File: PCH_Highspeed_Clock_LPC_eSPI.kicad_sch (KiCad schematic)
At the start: 3 parts

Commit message: Restructured schematic
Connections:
- net PCH_x4_Refclk-: now reaches UPCH1.AE14 (CLKOUT_PCIE_N2)
- net PCH_x4_Refclk+: now reaches UPCH1.AE15 (CLKOUT_PCIE_P2)
- net PCH_x4_CLKREQ#: now reaches UPCH1.AR32 (GPP_B7/SRCCLKREQ2#)
- net PCH_x4_PCIe_Tx0+: now reaches UPCH1.F46 (PCIE21_TXP)
- net PCH_x4_PCIe_Tx3+: now reaches UPCH1.G45 (PCIE24_TXP)
- net PCH_x4_PCIe_Tx3-: now reaches UPCH1.G46 (PCIE24_TXN)
- net PCH_x4_PCIe_Tx0-: now reaches UPCH1.G47 (PCIE21_TXN)
- net PCH_x4_PCIe_Tx2+: now reaches UPCH1.G48 (PCIE23_TXP)
- net PCH_x4_PCIe_Tx2-: now reaches UPCH1.G49 (PCIE23_TXN)
- net PCH_x4_PCIe_Tx1-: now reaches UPCH1.H47 (PCIE22_TXN)
- net PCH_x4_PCIe_Tx1+: now reaches UPCH1.H48 (PCIE22_TXP)
- net PCH_x4_PCIe_Rx0+: now reaches UPCH1.R44 (PCIE21_RXP)
- net PCH_x4_PCIe_Rx0-: now reaches UPCH1.T43 (PCIE21_RXN)
- net PCH_x4_PCIe_Rx1-: now reaches UPCH1.U40 (PCIE22_RXN)
- net PCH_x4_PCIe_Rx1+: now reaches UPCH1.U41 (PCIE22_RXP)
- net PCH_x4_PCIe_Rx2-: now reaches UPCH1.W43 (PCIE23_RXN)
- net PCH_x4_PCIe_Rx2+: now reaches UPCH1.W44 (PCIE23_RXP)
- net PCH_x4_PCIe_Rx3-: now reaches UPCH1.Y40 (PCIE24_RXN)
- net PCH_x4_PCIe_Rx3+: now reaches UPCH1.Y41 (PCIE24_RXP)
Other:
- note added: "Keep CLKREQ# and Refclk+/- paired!"
- note added: "subtract 5 for PCIe lane number (first 6 lanes are the USB3.1G2 ports + index starts at 0 vs 1)"
- note removed: "subtract 5 for PCIe lane number (first 6 lanes are the USB3.2G2 ports + index starts at 0 vs 1)"

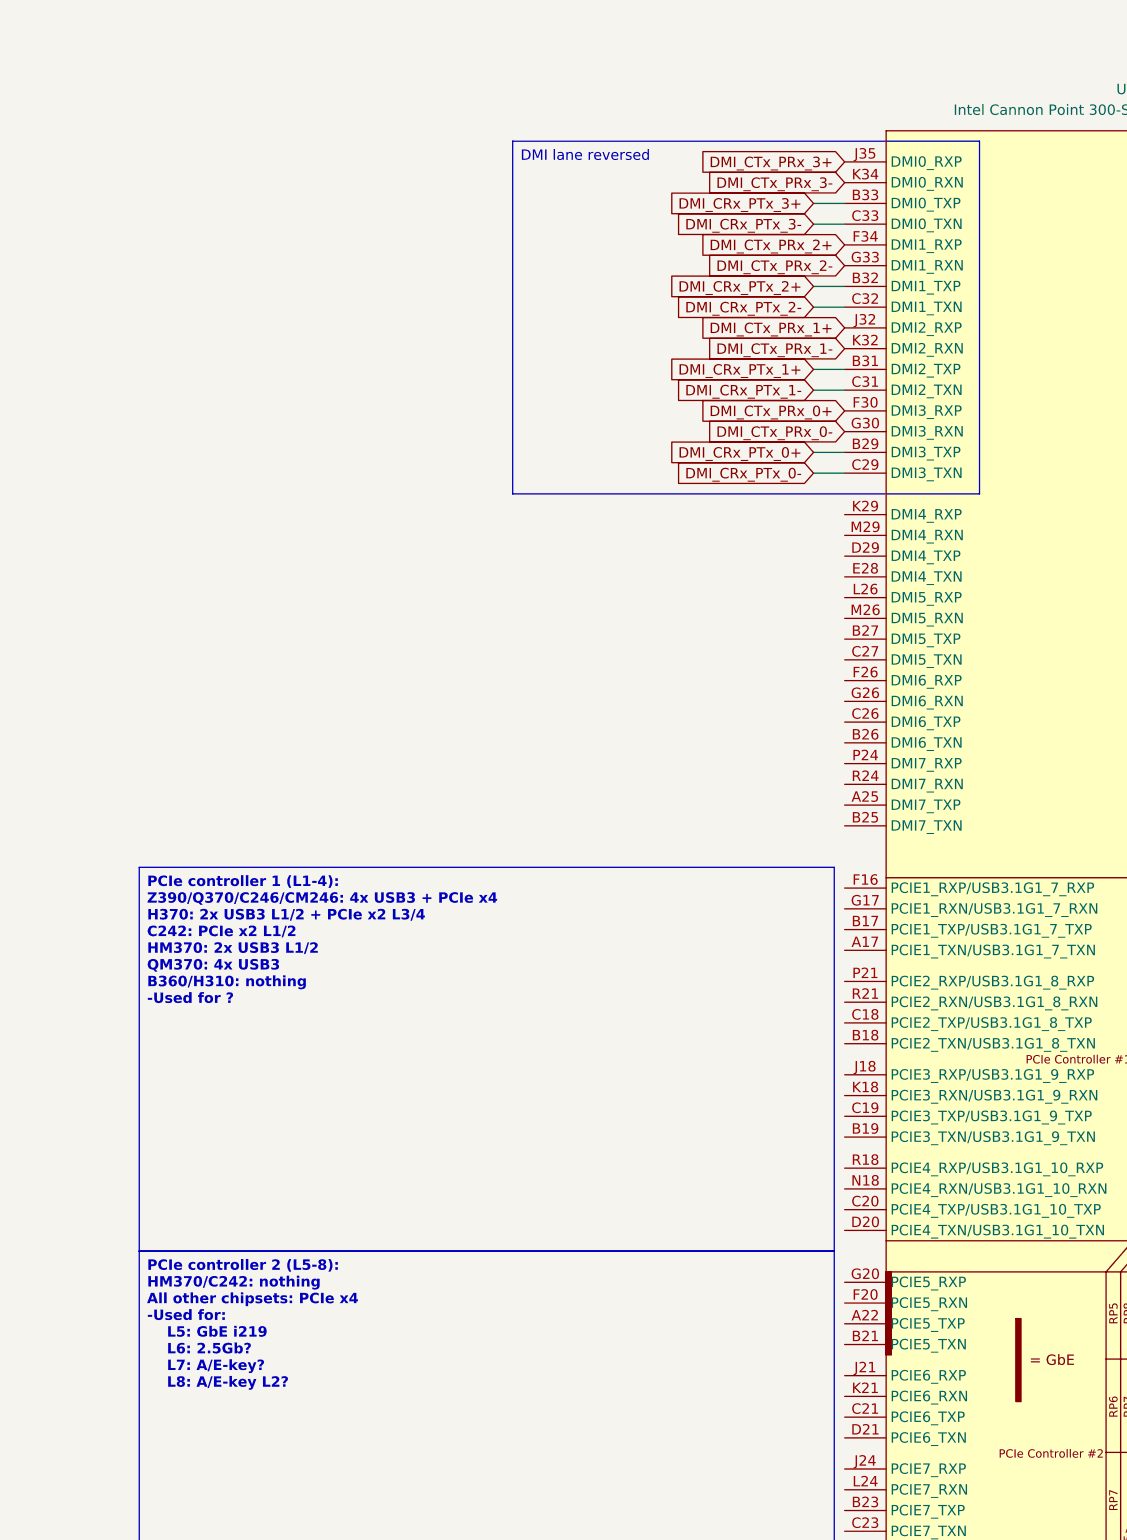
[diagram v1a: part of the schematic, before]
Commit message: Added interconnect between CPU and PCH boards and added ATX board outline
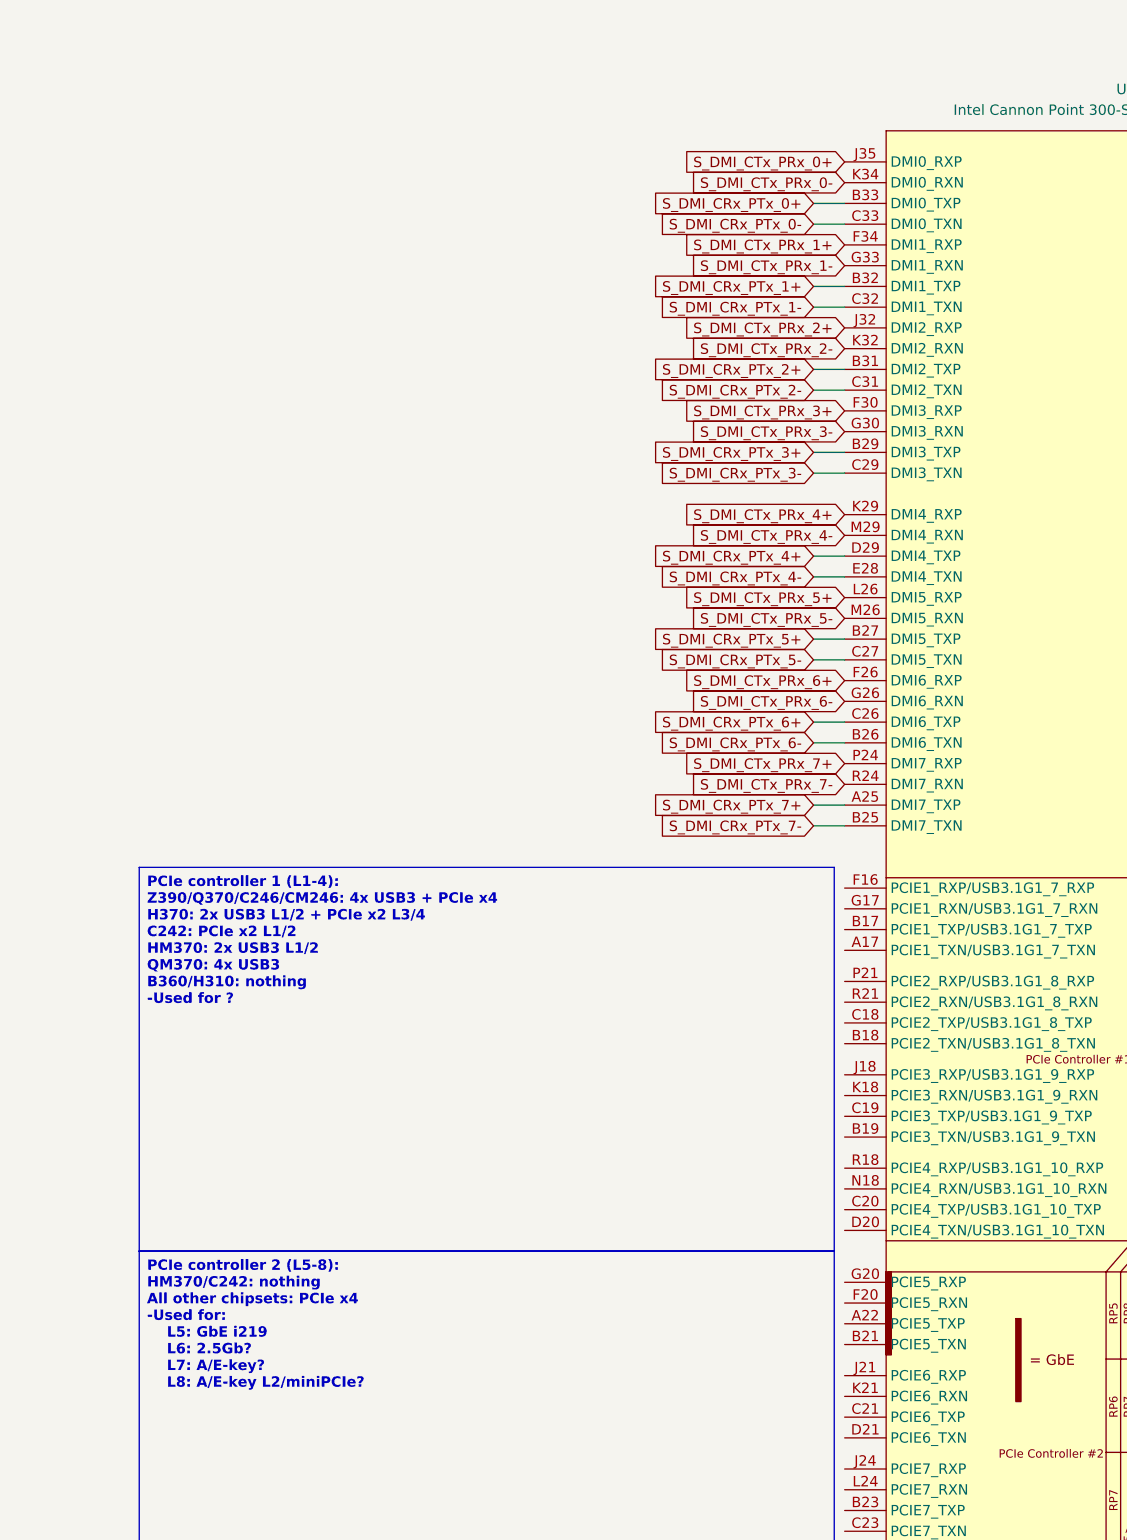
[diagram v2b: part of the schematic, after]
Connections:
- net S_DMI_CRx_PTx_7+: now reaches UPCH1.A25 (DMI7_TXP)
- net S_DMI_CRx_PTx_7-: now reaches UPCH1.B25 (DMI7_TXN)
- net S_DMI_CRx_PTx_6-: now reaches UPCH1.B26 (DMI6_TXN)
- net S_DMI_CRx_PTx_5+: now reaches UPCH1.B27 (DMI5_TXP)
- net S_DMI_CRx_PTx_6+: now reaches UPCH1.C26 (DMI6_TXP)
- net S_DMI_CRx_PTx_5-: now reaches UPCH1.C27 (DMI5_TXN)
- net S_DMI_CRx_PTx_4+: now reaches UPCH1.D29 (DMI4_TXP)
- net S_DMI_CRx_PTx_4-: now reaches UPCH1.E28 (DMI4_TXN)
- net S_DMI_CTx_PRx_6+: now reaches UPCH1.F26 (DMI6_RXP)
- net S_DMI_CTx_PRx_6-: now reaches UPCH1.G26 (DMI6_RXN)
- net S_DMI_CTx_PRx_4+: now reaches UPCH1.K29 (DMI4_RXP)
- net S_DMI_CTx_PRx_5+: now reaches UPCH1.L26 (DMI5_RXP)
- net S_DMI_CTx_PRx_5-: now reaches UPCH1.M26 (DMI5_RXN)
- net S_DMI_CTx_PRx_4-: now reaches UPCH1.M29 (DMI4_RXN)
- net S_DMI_CTx_PRx_7+: now reaches UPCH1.P24 (DMI7_RXP)
- net S_DMI_CTx_PRx_7-: now reaches UPCH1.R24 (DMI7_RXN)
- net DMI_CRx_PTx_0+ renamed S_DMI_CRx_PTx_3+
- net DMI_CRx_PTx_0- renamed S_DMI_CRx_PTx_3-
- net DMI_CRx_PTx_1+ renamed S_DMI_CRx_PTx_2+
- net DMI_CRx_PTx_1- renamed S_DMI_CRx_PTx_2-
- net DMI_CRx_PTx_2+ renamed S_DMI_CRx_PTx_1+
- net DMI_CRx_PTx_2- renamed S_DMI_CRx_PTx_1-
- net DMI_CRx_PTx_3+ renamed S_DMI_CRx_PTx_0+
- net DMI_CRx_PTx_3- renamed S_DMI_CRx_PTx_0-
- net DMI_CTx_PRx_0+ renamed S_DMI_CTx_PRx_3+
- net DMI_CTx_PRx_0- renamed S_DMI_CTx_PRx_3-
- net DMI_CTx_PRx_1+ renamed S_DMI_CTx_PRx_2+
- net DMI_CTx_PRx_1- renamed S_DMI_CTx_PRx_2-
- net DMI_CTx_PRx_2+ renamed S_DMI_CTx_PRx_1+
- net DMI_CTx_PRx_2- renamed S_DMI_CTx_PRx_1-
- net DMI_CTx_PRx_3+ renamed S_DMI_CTx_PRx_0+
- net DMI_CTx_PRx_3- renamed S_DMI_CTx_PRx_0-

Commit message: Added more PCIe slots and mounting holes
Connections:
- net PCH_x4_1_Refclk-: now reaches UPCH1.AB2 (CLKOUT_PCIE_N5)
- net PCH_x4_1_Refclk+: now reaches UPCH1.AB3 (CLKOUT_PCIE_P5)
- net PCH_x4_4_Refclk-: now reaches UPCH1.AC2 (CLKOUT_PCIE_N4)
- net PCH_x4_4_Refclk+: now reaches UPCH1.AC3 (CLKOUT_PCIE_P4)
- net PCH_x4_5_Refclk-: now reaches UPCH1.AE6 (CLKOUT_PCIE_N3)
- net PCH_x4_5_Refclk+: now reaches UPCH1.AE7 (CLKOUT_PCIE_P3)
- net PCH_x4_1_CLKREQ#: now reaches UPCH1.AN29 (GPP_B10/SRCCLKREQ5#)
- net PCH_x4_4_CLKREQ#: now reaches UPCH1.BA30 (GPP_B9/SRCCLKREQ4#)
- net PCH_x4_5_CLKREQ#: now reaches UPCH1.BB30 (GPP_B8/SRCCLKREQ3#)
- net PCH_x4_5_PCIe_Tx0-: now reaches UPCH1.A42 (PCIE17_TXN/SATA4_TXN)
- net PCH_x4_5_PCIe_Tx3-: now reaches UPCH1.A44 (PCIE20_TXN/SATA7_TXN)
- net PCH_x4_4_PCIe_Rx0-: now reaches UPCH1.B38 (PCIE13_TXN/SATA0B_TXN)
- net PCH_x4_4_PCIe_Rx2-: now reaches UPCH1.B40 (PCIE15_TXN/SATA2_TXN)
- net PCH_x4_4_PCIe_Rx3-: now reaches UPCH1.B41 (PCIE16_TXN/SATA3_TXN)
- net PCH_x4_5_PCIe_Tx0+: now reaches UPCH1.B42 (PCIE17_TXP/SATA4_TXP)
- net PCH_x4_5_PCIe_Tx3+: now reaches UPCH1.B44 (PCIE20_TXP/SATA7_TXP)
- net PCH_x4_4_PCIe_Rx0+: now reaches UPCH1.C38 (PCIE13_TXP/SATA0B_TXP)
- net PCH_x4_4_PCIe_Rx1-: now reaches UPCH1.C39 (PCIE14_TXN/SATA1B_TXN)
- net PCH_x4_4_PCIe_Rx2+: now reaches UPCH1.C40 (PCIE15_TXP/SATA2_TXP)
- net PCH_x4_4_PCIe_Rx3+: now reaches UPCH1.C41 (PCIE16_TXP/SATA3_TXP)
- net PCH_x4_5_PCIe_Tx1-: now reaches UPCH1.C42 (PCIE18_TXN/SATA5_TXN)
- net PCH_x4_5_PCIe_Tx2-: now reaches UPCH1.C44 (PCIE19_TXN/SATA6_TXN)
- net PCH_x4_4_PCIe_Tx0-: now reaches UPCH1.C45 (PCIE13_RXN/SATA0B_RXN)
- net PCH_x4_4_PCIe_Tx0+: now reaches UPCH1.C46 (PCIE13_RXP/SATA0B_RXP)
- net PCH_x4_4_PCIe_Tx1+: now reaches UPCH1.C47 (PCIE14_RXP/SATA1B_RXP)
- net PCH_x4_4_PCIe_Rx1+: now reaches UPCH1.D39 (PCIE14_TXP/SATA1B_TXP)
- net PCH_x4_5_PCIe_Tx1+: now reaches UPCH1.D42 (PCIE18_TXP/SATA5_TXP)
- net PCH_x4_5_PCIe_Tx2+: now reaches UPCH1.D43 (PCIE19_TXP/SATA6_TXP)
- net PCH_x4_4_PCIe_Tx1-: now reaches UPCH1.D46 (PCIE14_RXN/SATA1B_RXN)
- net PCH_x4_4_PCIe_Tx2+: now reaches UPCH1.E45 (PCIE15_RXP/SATA2_RXP)
- net PCH_x4_4_PCIe_Tx2-: now reaches UPCH1.F44 (PCIE15_RXN/SATA2_RXN)
- net PCH_x4_5_PCIe_Rx0-: now reaches UPCH1.K43 (PCIE17_RXN/SATA4_RXN)
- net PCH_x4_5_PCIe_Rx0+: now reaches UPCH1.K44 (PCIE17_RXP/SATA4_RXP)
- net PCH_x4_4_PCIe_Tx3-: now reaches UPCH1.L41 (PCIE16_RXN/SATA3_RXN)
- net PCH_x4_4_PCIe_Tx3+: now reaches UPCH1.M40 (PCIE16_RXP/SATA3_RXP)
- net PCH_x4_5_PCIe_Rx2-: now reaches UPCH1.M44 (PCIE19_RXN/SATA6_RXN)
- net PCH_x4_5_PCIe_Rx2+: now reaches UPCH1.N42 (PCIE19_RXP/SATA6_RXP)
- net PCH_x4_5_PCIe_Rx1-: now reaches UPCH1.P41 (PCIE18_RXN/SATA5_RXN)
- net PCH_x4_5_PCIe_Rx3-: now reaches UPCH1.R35 (PCIE20_RXN/SATA7_RXN)
- net PCH_x4_5_PCIe_Rx3+: now reaches UPCH1.R37 (PCIE20_RXP/SATA7_RXP)
- net PCH_x4_5_PCIe_Rx1+: now reaches UPCH1.R40 (PCIE18_RXP/SATA5_RXP)
- net PCH_x4_1_PCIe_Tx0-: now reaches UPCH1.A17 (PCIE1_TXN/USB3.1G1_7_TXN)
- net PCH_x4_1_PCIe_Tx0+: now reaches UPCH1.B17 (PCIE1_TXP/USB3.1G1_7_TXP)
- net PCH_x4_1_PCIe_Tx1-: now reaches UPCH1.B18 (PCIE2_TXN/USB3.1G1_8_TXN)
- net PCH_x4_1_PCIe_Tx2-: now reaches UPCH1.B19 (PCIE3_TXN/USB3.1G1_9_TXN)
- net PCH_x4_1_PCIe_Tx1+: now reaches UPCH1.C18 (PCIE2_TXP/USB3.1G1_8_TXP)
- net PCH_x4_1_PCIe_Tx2+: now reaches UPCH1.C19 (PCIE3_TXP/USB3.1G1_9_TXP)
- net PCH_x4_1_PCIe_Tx3+: now reaches UPCH1.C20 (PCIE4_TXP/USB3.1G1_10_TXP)
- net PCH_x4_1_PCIe_Tx3-: now reaches UPCH1.D20 (PCIE4_TXN/USB3.1G1_10_TXN)
- net PCH_x4_1_PCIe_Rx0+: now reaches UPCH1.F16 (PCIE1_RXP/USB3.1G1_7_RXP)
- net PCH_x4_1_PCIe_Rx0-: now reaches UPCH1.G17 (PCIE1_RXN/USB3.1G1_7_RXN)
- net PCH_x4_1_PCIe_Rx2+: now reaches UPCH1.J18 (PCIE3_RXP/USB3.1G1_9_RXP)
- net PCH_x4_1_PCIe_Rx2-: now reaches UPCH1.K18 (PCIE3_RXN/USB3.1G1_9_RXN)
- net PCH_x4_1_PCIe_Rx3-: now reaches UPCH1.N18 (PCIE4_RXN/USB3.1G1_10_RXN)
- net PCH_x4_1_PCIe_Rx1+: now reaches UPCH1.P21 (PCIE2_RXP/USB3.1G1_8_RXP)
- net PCH_x4_1_PCIe_Rx3+: now reaches UPCH1.R18 (PCIE4_RXP/USB3.1G1_10_RXP)
- net PCH_x4_1_PCIe_Rx1-: now reaches UPCH1.R21 (PCIE2_RXN/USB3.1G1_8_RXN)
- net PCH_x4_CLKREQ# renamed PCH_x4_6_CLKREQ#
- net PCH_x4_PCIe_Rx0+ renamed PCH_x4_6_PCIe_Rx0+
- net PCH_x4_PCIe_Rx0- renamed PCH_x4_6_PCIe_Rx0-
- net PCH_x4_PCIe_Rx1+ renamed PCH_x4_6_PCIe_Rx1+
- net PCH_x4_PCIe_Rx1- renamed PCH_x4_6_PCIe_Rx1-
- net PCH_x4_PCIe_Rx2+ renamed PCH_x4_6_PCIe_Rx2+
- net PCH_x4_PCIe_Rx2- renamed PCH_x4_6_PCIe_Rx2-
- net PCH_x4_PCIe_Rx3+ renamed PCH_x4_6_PCIe_Rx3+
- net PCH_x4_PCIe_Rx3- renamed PCH_x4_6_PCIe_Rx3-
- net PCH_x4_PCIe_Tx0+ renamed PCH_x4_6_PCIe_Tx0+
- net PCH_x4_PCIe_Tx0- renamed PCH_x4_6_PCIe_Tx0-
- net PCH_x4_PCIe_Tx1+ renamed PCH_x4_6_PCIe_Tx1+
- net PCH_x4_PCIe_Tx1- renamed PCH_x4_6_PCIe_Tx1-
- net PCH_x4_PCIe_Tx2+ renamed PCH_x4_6_PCIe_Tx2+
- net PCH_x4_PCIe_Tx2- renamed PCH_x4_6_PCIe_Tx2-
- net PCH_x4_PCIe_Tx3+ renamed PCH_x4_6_PCIe_Tx3+
- net PCH_x4_PCIe_Tx3- renamed PCH_x4_6_PCIe_Tx3-
- net PCH_x4_Refclk+ renamed PCH_x4_6_Refclk+
- net PCH_x4_Refclk- renamed PCH_x4_6_Refclk-
- net SSD0_PCIe/SATA_Rx0+ renamed SSD0_SATA/PCIe_Rx0+
- net SSD0_PCIe/SATA_Rx0- renamed SSD0_SATA/PCIe_Rx0-
- net SSD0_PCIe/SATA_Tx0+ renamed SSD0_SATA/PCIe_Tx0+
- net SSD0_PCIe/SATA_Tx0- renamed SSD0_SATA/PCIe_Tx0-
